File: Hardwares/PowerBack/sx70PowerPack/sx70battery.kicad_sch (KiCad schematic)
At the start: 42 parts, among them J1 USB_C_Receptacle_PowerOnly_6P, U1 TP4057, U3 LN60A, U4 TPS61085DGK

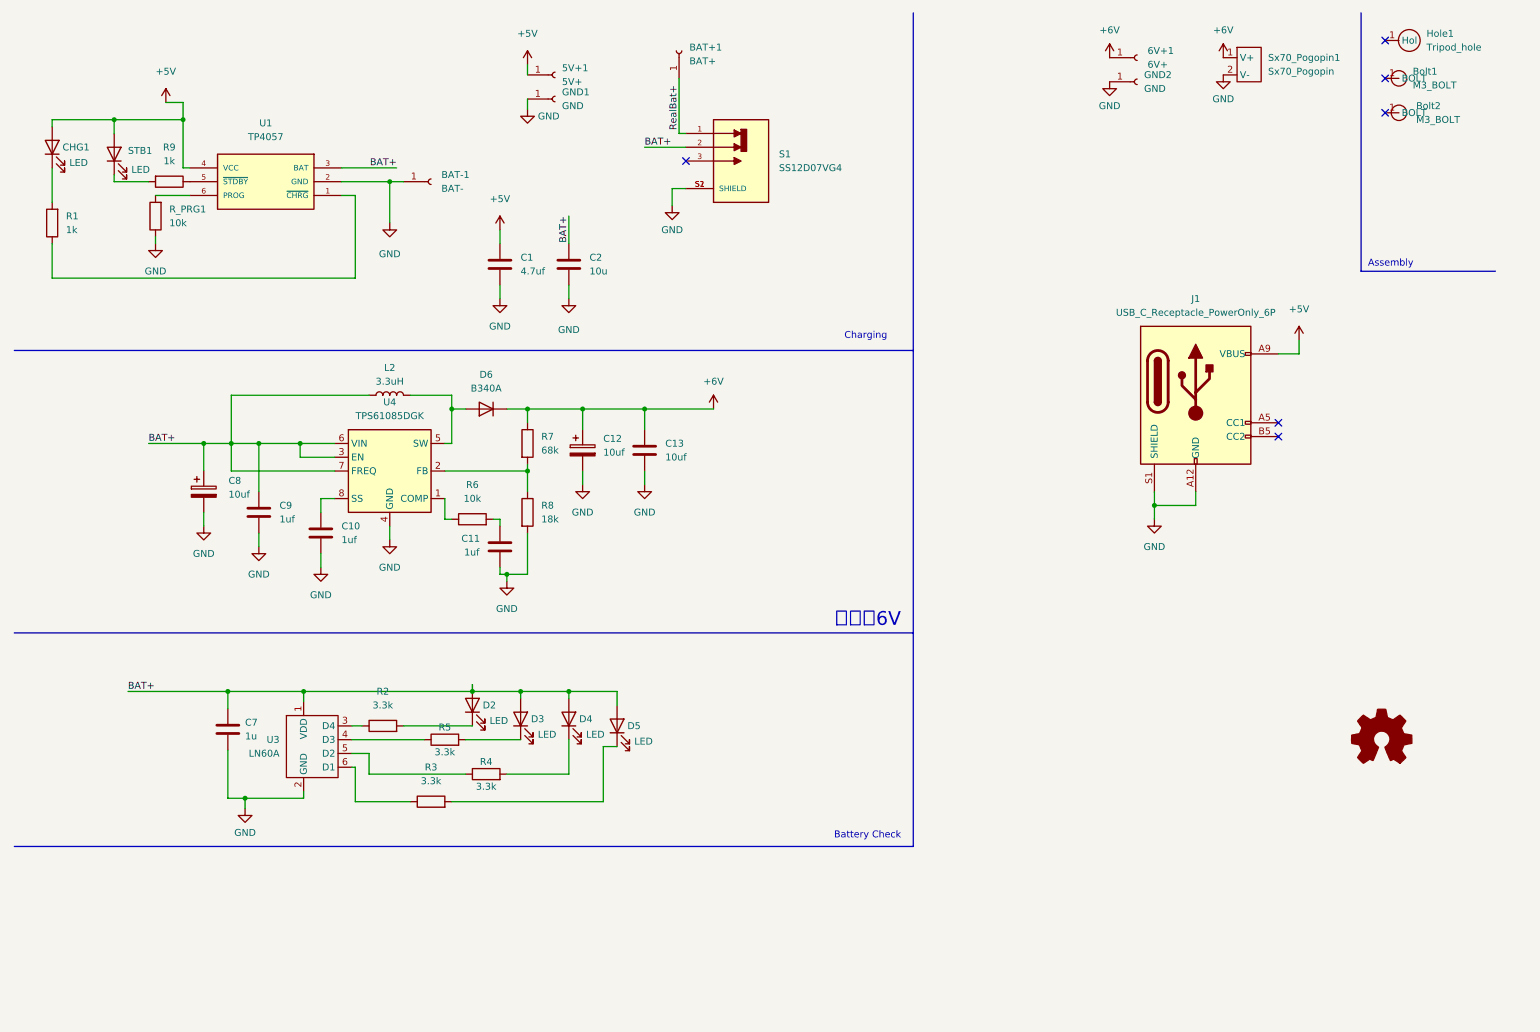
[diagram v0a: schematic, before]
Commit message: 外置电池设计完毕，生成光绘文件
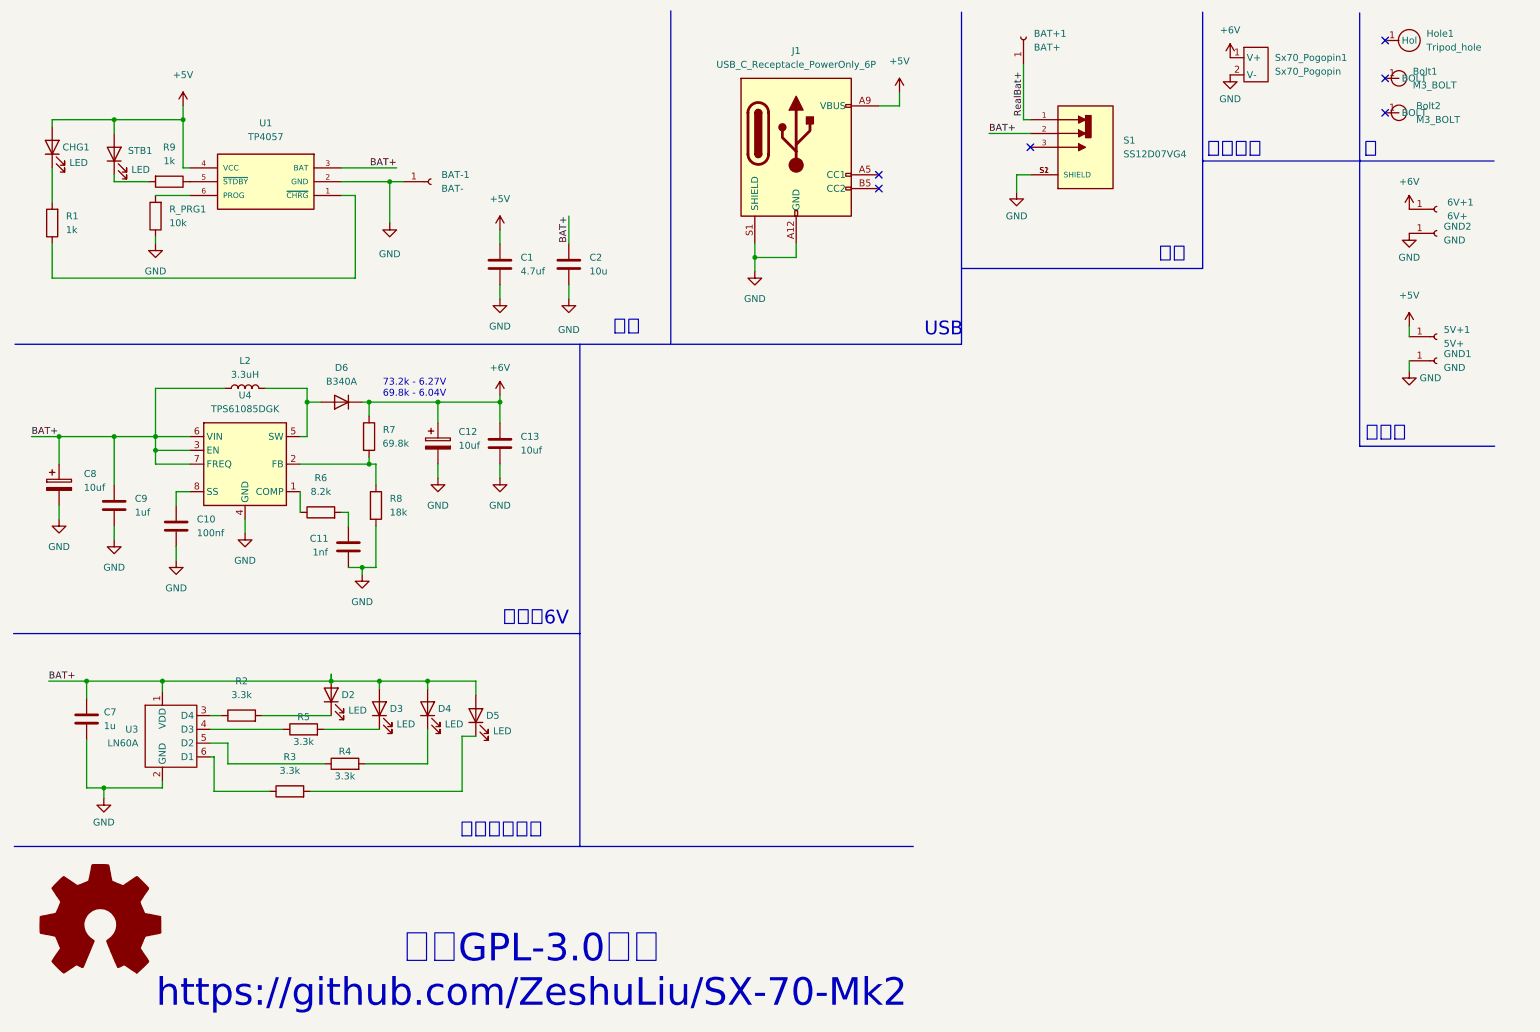
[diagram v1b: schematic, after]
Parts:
- C10: value 1uf -> 100nf
- C11: value 1uf -> 1nf
- R6: value 10k -> 8.2k
- R7: value 68k -> 69.8k
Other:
- note added: "73.2k - 6.27V 69.8k - 6.04V"
- note added: "USB"
- note added: "使用GPL-3.0许可 https://github.com/ZeshuLiu/SX-70-Mk2"
- note added: "充电"
- note added: "孔"
- note added: "开关"
- note added: "测试点"
- note added: "电池升6V"
- note added: "电池电量检测"
- note added: "相机供电"
- note removed: "Assembly"
- note removed: "Battery Check"
- note removed: "Charging"
- note removed: "电池转6V"
- company: ZS Liu -> SX-70 Mk2 Project
- moved on the sheet: 5V+1, 6V+1, BAT+1, C10, C11, C12, C13, C7, C8, C9, D2, D3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

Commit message: 电池2.1版本（CC识别可以充电）
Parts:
- added R10, R11: 5.1k, Resistor_SMD:R_0603_1608Metric_Pad0.98x0.95mm_HandSolder, symbol Device:R
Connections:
- net GND: now also R10.1, R11.1
- net at J1.A5 (CC1): now also R11.2
- net at J1.B5 (CC2): now also R10.2
- no-connect marks 6 -> 4
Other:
- moved on the sheet: J1

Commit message: 代码OK，电屁股正在做
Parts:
- removed C10: 100nf, Capacitor_SMD:C_0603_1608Metric_Pad1.08x0.95mm_HandSolder, symbol Device:C
- removed C11: 1nf, Capacitor_SMD:C_0603_1608Metric_Pad1.08x0.95mm_HandSolder, symbol Device:C
- removed C12, C8: 10uf, Capacitor_Tantalum_SMD:CP_EIA-3216-18_Kemet-A, symbol Device:C_Polarized
- removed C13: 10uf, Capacitor_SMD:C_0805_2012Metric_Pad1.18x1.45mm_HandSolder, symbol Device:C
- removed C9: 1uf, Capacitor_SMD:C_0603_1608Metric_Pad1.08x0.95mm_HandSolder, symbol Device:C
- removed D6: B340A, Diode_SMD:D_SMA, symbol Device:D
- removed L2: 3.3uH, Inductor_SMD:L_Cenker_CKCS6020, symbol Device:L
- removed R6: 8.2k, Resistor_SMD:R_0603_1608Metric_Pad0.98x0.95mm_HandSolder, symbol Device:R
- removed R7: 69.8k, Resistor_SMD:R_0603_1608Metric_Pad0.98x0.95mm_HandSolder, symbol Device:R
- removed R8: 18k, Resistor_SMD:R_0603_1608Metric_Pad0.98x0.95mm_HandSolder, symbol Device:R
- removed U4: TPS61085DGK, Package_SO:VSSOP-8_3.0x3.0mm_P0.65mm, symbol Regulator_Switching:TPS61085DGK
- added C3: 100nf, Capacitor_SMD:C_0603_1608Metric, symbol Device:C
- added C4: 1uf, Capacitor_SMD:C_1206_3216Metric_Pad1.33x1.80mm_HandSolder, symbol Device:C
- added C5: 10uf, Capacitor_SMD:C_1206_3216Metric_Pad1.33x1.80mm_HandSolder, symbol Device:C
- added D1: SS34, Diode_SMD:D_SMA, symbol Diode:SS34
- added D7: 1N5819WS, Diode_SMD:D_SOD-323_HandSoldering, symbol Diode:1N5819WS
- added L1: 4.7uH, Inductor_SMD:L_APV_APH0650, symbol Device:L
- added R12: 100, Resistor_SMD:R_0603_1608Metric_Pad0.98x0.95mm_HandSolder, symbol Device:R
- added R13: 1k, Resistor_SMD:R_0603_1608Metric_Pad0.98x0.95mm_HandSolder, symbol Device:R
- added R15: 330k, Resistor_SMD:R_0603_1608Metric_Pad0.98x0.95mm_HandSolder, symbol Device:R
- added R16: 51k, Resistor_SMD:R_0603_1608Metric_Pad0.98x0.95mm_HandSolder, symbol Device:R
- added U2: DW01A, Package_TO_SOT_SMD:SOT-23-6, symbol Battery_Management:DW01A
- added U5, U6, U7, U8: ~, Package_SO:TSSOP-8_4.4x3mm_P0.65mm, symbol KiCadLib:8205A
- added U9: TLV61048DBVR, Package_TO_SOT_SMD:SOT-23-6, symbol 2025-04-10_12-12-53:TLV61048DBVR
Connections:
- net +6V: now also C5.1, D1.1 (K), D7.1 (K), R15.1
- net BAT+: now also C4.1, L1.1, U9.4 (EN), U9.5 (VIN)
- net GND: now also C4.2, C5.2, D7.2 (A), R13.1, R16.2, U5.6 (S2), U5.7 (S2), U6.6 (S2), U6.7 (S2), U7.6 (S2), U7.7 (S2), U8.6 (S2), U8.7 (S2), U9.2 (GND); no longer BAT-1.1 (Pin_1), U1.2 (GND)
- net RealBat+: now also R12.1
- new net: R15.2, R16.1, U9.3 (FB)
- new net: U7.1 (D1), U7.8 (D2)
- new net: U2.1 (OD), U5.4 (G1), U6.4 (G1), U7.4 (G1), U8.4 (G1)
- new net: U2.3 (OC), U5.5 (G2), U6.5 (G2), U7.5 (G2), U8.5 (G2)
- new net: U8.1 (D1), U8.8 (D2)
- new net: R13.2, U2.2 (CS)
- new net: C3.1, R12.2, U2.5 (VCC)
- new net: U5.1 (D1), U5.8 (D2)
- new net: U6.1 (D1), U6.8 (D2)
- new net RealBat-: BAT-1.1 (Pin_1), C3.2, U1.2 (GND), U2.6 (GND), U5.2 (S1), U5.3 (S1), U6.2 (S1), U6.3 (S1), U7.2 (S1), U7.3 (S1), U8.2 (S1), U8.3 (S1)
- new net SW: D1.2 (A), L1.2, U9.1 (SW)
- no-connect marks 4 -> 5
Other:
- note removed: "73.2k - 6.27V 69.8k - 6.04V"

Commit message: 声纳工作正常
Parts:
- added Bolt3, Bolt4: M3_BOLT, MountingHole:MountingHole_3.2mm_M3_Pad, symbol Jimmy_Library:M3_BOLT
- added C10: 1uf, Capacitor_SMD:C_0603_1608Metric, symbol Device:C
- added C11: 22nf, Capacitor_SMD:C_0603_1608Metric, symbol Device:C
- added C12: 2nf, Capacitor_SMD:C_0603_1608Metric, symbol Device:C
- added C13, C8: 100nf, Capacitor_SMD:C_0603_1608Metric, symbol Device:C
- added C6: 22uf, Capacitor_SMD:C_1206_3216Metric_Pad1.33x1.80mm_HandSolder, symbol Device:C
- added C9: 47uf, Capacitor_SMD:C_1206_3216Metric_Pad1.33x1.80mm_HandSolder, symbol Device:C
- added D6: SS34, Diode_SMD:D_SMA, symbol Diode:SS34
- added L2: 3.3uH, Inductor_SMD:L_APV_APH0650, symbol Device:L
- added R14: 866, Resistor_SMD:R_0603_1608Metric_Pad0.98x0.95mm_HandSolder, symbol Device:R
- added R6: 39k, Resistor_SMD:R_0603_1608Metric_Pad0.98x0.95mm_HandSolder, symbol Device:R
- added R7: 10k, Resistor_SMD:R_0603_1608Metric_Pad0.98x0.95mm_HandSolder, symbol Device:R
- added R8: 60.4k, Resistor_SMD:R_0603_1608Metric_Pad0.98x0.95mm_HandSolder, symbol Device:R
- added U4: ~, Package_SO:HTSSOP-14-1EP_4.4x5mm_P0.65mm_EP3.4x5mm_Mask3x3.1mm, symbol KiCadLib:TPS55340
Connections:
- net +6V: now also C10.1, C9.1, D6.1 (K), R6.1
- net BAT+: now also C6.1, C8.1, L2.1, U4.3 (Vin), U4.4 (EN); no longer C2.1, U1.3 (BAT)
- net GND: now also U1.2 (GND), C10.2, C11.2, C12.2, C13.2, C6.2, C8.2, C9.2, R7.2, R8.2, U4.12 (PGND), U4.13 (PGND), U4.14 (PGND), U4.15 (EP), U4.6 (SYNC), U4.7 (AGND)
- net RealBat+: now also C2.1, U1.3 (BAT)
- net RealBat-: no longer U1.2 (GND)
- net at U7.1 (D1): no longer U7.8 (D2)
- net at U8.1 (D1): no longer U8.8 (D2)
- net at U5.1 (D1): no longer U5.8 (D2)
- net at U6.1 (D1): no longer U6.8 (D2)
- new net: D6.2 (A), L2.2, U4.1 (SW), U4.2 (SW)
- new net: R8.1, U4.10 (FREQ)
- new net: C11.1, U4.5 (SS)
- new net: C12.1, R14.1, U4.8 (COMP)
- new net: R6.2, R7.1, U4.9 (FB)
- new net: C13.1, R14.2
- no-connect marks 5 -> 15
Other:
- note added: "电池保护"
- note added: "电池升压6V-备用"
- moved on the sheet: BAT-1, Bolt1, Bolt2, C3, Hole1, R12, R13, U2, U5, U6, U7, U8
